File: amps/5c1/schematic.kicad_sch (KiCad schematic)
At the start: 21 parts, among them T1 SE 5k:8

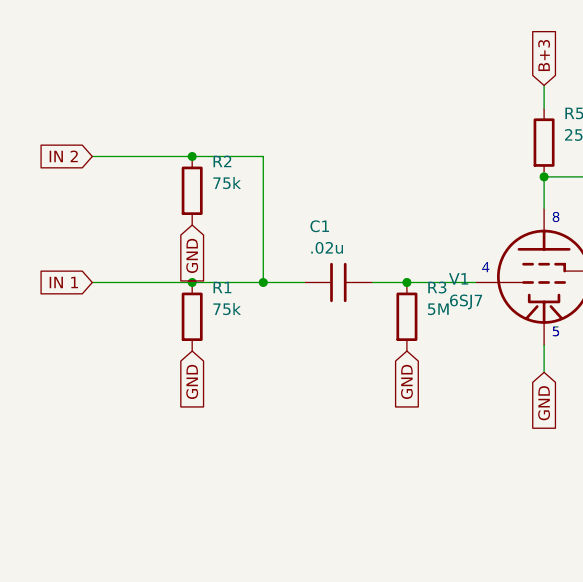
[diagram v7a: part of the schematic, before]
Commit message: 5C1: input 75 kΩ resistors are in series, not shunts to ground (V1 audit)
F-DH draws each 75 K in series from its jack's tip to the summing node
ahead of the .02 coupler, on both pages (hi-res capture, schematic page
5770x4632 crop 50,1300,1100,900; layout page 6510x4718 crop
400,3300,1300,1100; the cited two-page copy, 1159x958 / 1295x982, shows
the same). Both the sheet and the board drew them as shunts to ground with
the jacks tied straight to C1 — an error shared by both surfaces, so the
sheet-board gate could not see it. Jack 1's grounding contact is noted in
the comments but not drawn (glabel inputs; no board terminal).

BOM roles follow; the line cap is one AC leg to chassis on the line side
of the fuse, not "across the line". Notes corrected. The input network is
outside the DC deck: no netlist or chart change.

Co-Authored-By: Claude Opus 5.5 <noreply@anthropic.com>
Claude-Session: https://claude.ai/code/session_01KBMfdh37HmCL2iWcBiL5J1
Signed-off-by: AnalogMaker <theanalogmaker@gmail.com>
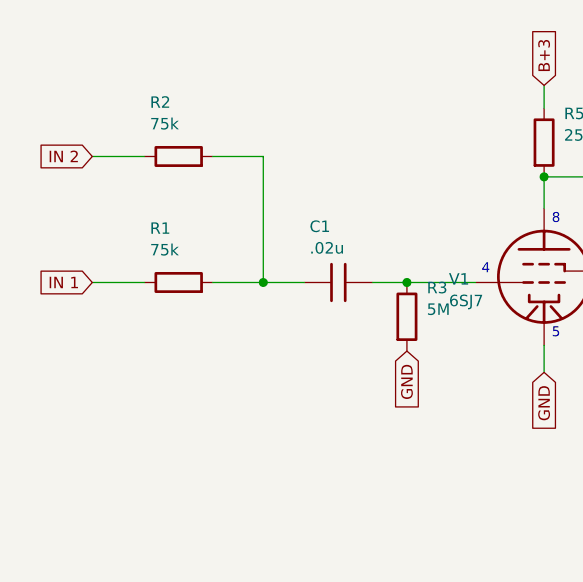
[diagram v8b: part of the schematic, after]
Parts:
- removed R3: 5M, symbol cx:R
- removed R5: 250k, symbol cx:R
- removed R6: 500, symbol cx:R
- removed T1: SE 5k:8, symbol cx:OT_SE
- removed V3B: 5Y3GT, symbol cx:DIODE_TUBE
- removed VR1: 1M vol, symbol cx:POT
- added C1: .02u, symbol cx:C
- added C4: 25u, symbol cx:C
- added R4: 2M, symbol cx:R
- added V1: 6SJ7, symbol cx:PENTODE
- added V2: 6V6GT, symbol cx:PENTODE
- added V3A: 5Y3GT, symbol cx:DIODE_TUBE
- R3: renamed from C1; value .02u -> 5M; symbol cx:C -> cx:R
- R5: renamed from V1; value 6SJ7 -> 250k; symbol cx:PENTODE -> cx:R
- R6: renamed from V2; value 6V6GT -> 500; symbol cx:PENTODE -> cx:R
- T1: renamed from C4; value 25u -> SE 5k:8; symbol cx:C -> cx:OT_SE
- VR1: renamed from R4; value 2M -> 1M vol; symbol cx:R -> cx:POT
- renumbered V3A to V3B
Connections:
- net B+1: now also V3A.2 (K)
- net B+2: now also T1.2 (PRI_B)
- net B+3: now also R5.1, R4.1, V2.3 (G2); no longer R6.3 (G2), VR1.1
- net GND: now also R3.2, R6.2, T1.4 (SEC_C), VR1.3, C4.2, V1.4 (K); no longer R1.2, R2.2, R5.4 (K), T1.2
- net HT_A: now also V3A.1 (A); no longer V3B.1 (A)
- net HT_B: now also V3B.1 (A)
- net IN 1: no longer R2.1, R3.1
- net SPKR: now also T1.3 (SEC_H)
- net at R5.2: now also C3.1, V1.1 (P); no longer R3.2
- net at R6.1: now also C4.1, V2.4 (K)
- net at T1.1 (PRI_P): now also V2.1 (P); no longer R6.4 (K)
- net at C3.2: now also VR1.1
- new net: C2.1, R4.2, V1.3 (G2)
- new net: C1.2, R3.1, V1.2 (G1)
- new net: C1.1, R1.2, R2.2
- new net: V2.2 (G1), VR1.2 (W)
- new net IN 2: R2.1
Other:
- moved on the sheet: V3B
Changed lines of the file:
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@@
   (global_label "IN 1" (shape input) (at 17.8816 38.913 180)
     (effects (font (size 1.27 1.27)) (justify right)))
-  (wire (pts (xy 17.8816 38.913) (xy 28.9816 38.913))
+  (symbol (lib_id "cx:R") (at 27.4816 38.913 90) (unit 1)
+    (in_bom yes) (on_board yes)
+    (property "Reference" "R1" (at 24.2816 32.913 270) (effects (font (size 1.27 1.27)) (justify left)))
+    (property "Value" "75k" (at 24.2816 35.313 270) (effects (font (size 1.27 1.27)) (justify left))))
+  (wire (pts (xy 17.8816 38.913) (xy 23.6716 38.913))
     (stroke (width 0) (type default)))
-  (junction (at 28.9816 38.913) (diameter 1) (color 0 0 0 0))
-  (symbol (lib_id "cx:R") (at 28.9816 42.723 0) (unit 1)
-    (in_bom yes) (on_board yes)
-    (property "Reference" "R1" (at 31.1816 39.523 0) (effects (font (size 1.27 1.27)) (justify left)))
-    (property "Value" "75k" (at 31.1816 41.923 0) (effects (font (size 1.27 1.27)) (justify left))))
-  (global_label "GND" (shape input) (at 28.9816 46.533 270)
-    (effects (font (size 1.27 1.27)) (justify right)))
-  (wire (pts (xy 28.9816 38.913) (xy 36.8816 38.913))
+  (wire (pts (xy 31.2916 38.913) (xy 36.8816 38.913))
     (stroke (width 0) (type default)))
   (global_label "IN 2" (shape input) (at 17.8816 24.913 180)
     (effects (font (size 1.27 1.27)) (justify right)))
-  (wire (pts (xy 17.8816 24.913) (xy 28.9816 24.913))
+  (symbol (lib_id "cx:R") (at 27.4816 24.913 90) (unit 1)
+    (in_bom yes) (on_board yes)
+    (property "Reference" "R2" (at 24.2816 18.913 270) (effects (font (size 1.27 1.27)) (justify left)))
+    (property "Value" "75k" (at 24.2816 21.313 270) (effects (font (size 1.27 1.27)) (justify left))))
+  (wire (pts (xy 17.8816 24.913) (xy 23.6716 24.913))
     (stroke (width 0) (type default)))
-  (junction (at 28.9816 24.913) (diameter 1) (color 0 0 0 0))
-  (symbol (lib_id "cx:R") (at 28.9816 28.723 0) (unit 1)
-    (in_bom yes) (on_board yes)
-    (property "Reference" "R2" (at 31.1816 25.523 0) (effects (font (size 1.27 1.27)) (justify left)))
-    (property "Value" "75k" (at 31.1816 27.923 0) (effects (font (size 1.27 1.27)) (justify left))))
-  (global_label "GND" (shape input) (at 28.9816 32.533 270)
-    (effects (font (size 1.27 1.27)) (justify right)))
-  (wire (pts (xy 28.9816 24.913) (xy 36.8816 24.913))
+  (wire (pts (xy 31.2916 24.913) (xy 36.8816 24.913))
     (stroke (width 0) (type default)))
   (wire (pts (xy 36.8816 24.913) (xy 36.8816 38.913))
